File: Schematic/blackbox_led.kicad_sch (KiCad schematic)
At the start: 26 parts, among them U6 CSNP1GCR01-BOW

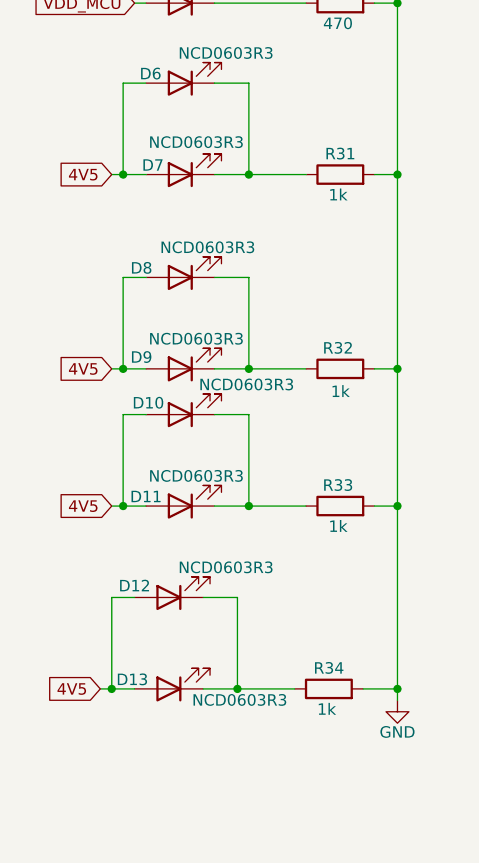
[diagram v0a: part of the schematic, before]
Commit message: optimisation : - refactoring two 4 pin connector for mag and gps into one 6 pin connector - increased output voltage from 5V buck regulator to take into account voltage decrease schottky diodes
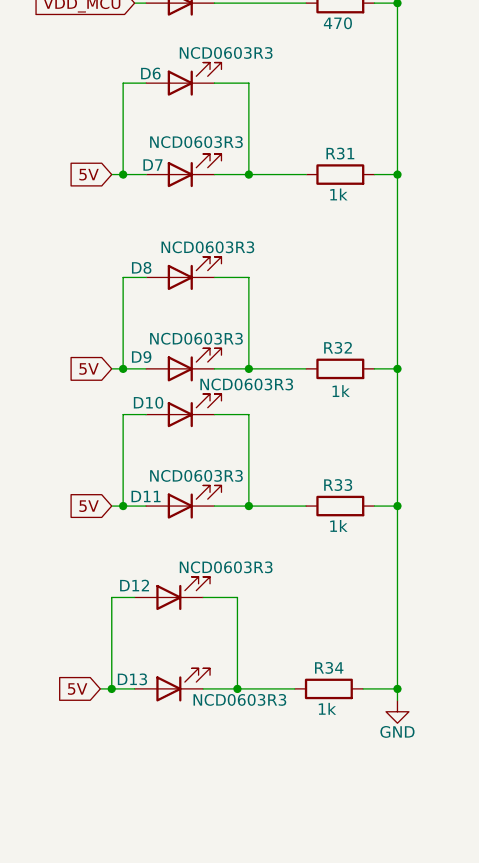
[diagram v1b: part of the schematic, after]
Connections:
- net 4V5 renamed 5V
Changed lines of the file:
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@@
 		)
 	)
-	(global_label "4V5"
+	(global_label "5V"
 		(shape input)
 		(at 58.42 97.79 180)
@@
 		)
 		(property "Intersheetrefs" "${INTERSHEET_REFS}"
-			(at 51.9272 97.79 0)
+			(at 53.1367 97.79 0)
 			(effects
 				(font
@@
 		)
 	)
-	(global_label "4V5"
+	(global_label "5V"
 		(shape input)
 		(at 58.42 119.38 180)
@@
 		)
 		(property "Intersheetrefs" "${INTERSHEET_REFS}"
-			(at 51.9272 119.38 0)
+			(at 53.1367 119.38 0)
 			(effects
 				(font
@@
 		)
 	)
-	(global_label "4V5"
+	(global_label "5V"
 		(shape input)
 		(at 57.15 154.94 180)
@@
 		)
 		(property "Intersheetrefs" "${INTERSHEET_REFS}"
-			(at 50.6572 154.94 0)
+			(at 51.8667 154.94 0)
 			(effects
 				(font
@@
 		)
 	)
-	(global_label "4V5"
+	(global_label "5V"
 		(shape input)
 		(at 58.42 134.62 180)
@@
 		)
 		(property "Intersheetrefs" "${INTERSHEET_REFS}"
-			(at 51.9272 134.62 0)
-			(effects
-				(font
+			(at 53.1367 134.62 0)
+			(effects
+				(font

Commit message: update on routing
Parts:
- C45, C46: footprint Capacitor_SMD:C_0603_1608Metric -> Capacitor_SMD:C_0402_1005Metric
- R28, R29, R30, R31, R32, R33, R34, R35, R36, R37, R38, R39: footprint Resistor_SMD:R_0603_1608Metric -> Resistor_SMD:R_0402_1005Metric
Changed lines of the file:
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@@
 			)
 		)
-		(property "Footprint" "Resistor_SMD:R_0603_1608Metric"
+		(property "Footprint" "Resistor_SMD:R_0402_1005Metric"
 			(at 232.918 109.22 90)
 			(effects
@@
 			)
 		)
-		(property "Footprint" "Resistor_SMD:R_0603_1608Metric"
+		(property "Footprint" "Resistor_SMD:R_0402_1005Metric"
 			(at 227.838 109.22 90)
 			(effects
@@
 			)
 		)
-		(property "Footprint" "Resistor_SMD:R_0603_1608Metric"
+		(property "Footprint" "Resistor_SMD:R_0402_1005Metric"
 			(at 83.82 136.398 90)
 			(effects
@@
 			)
 		)
-		(property "Footprint" "Resistor_SMD:R_0603_1608Metric"
+		(property "Footprint" "Resistor_SMD:R_0402_1005Metric"
 			(at 185.928 85.09 90)
 			(effects
@@
 			)
 		)
-		(property "Footprint" "Resistor_SMD:R_0603_1608Metric"
+		(property "Footprint" "Resistor_SMD:R_0402_1005Metric"
 			(at 82.55 156.718 90)
 			(effects
@@
 			)
 		)
-		(property "Footprint" "Resistor_SMD:R_0603_1608Metric"
+		(property "Footprint" "Resistor_SMD:R_0402_1005Metric"
 			(at 83.82 80.518 90)
 			(effects
@@
 			)
 		)
-		(property "Footprint" "Resistor_SMD:R_0603_1608Metric"
+		(property "Footprint" "Resistor_SMD:R_0402_1005Metric"
 			(at 83.82 58.928 90)
 			(effects
@@
 			)
 		)
-		(property "Footprint" "Resistor_SMD:R_0603_1608Metric"
+		(property "Footprint" "Resistor_SMD:R_0402_1005Metric"
 			(at 191.008 85.09 90)
 			(effects
@@
 			)
 		)
-		(property "Footprint" "Resistor_SMD:R_0603_1608Metric"
+		(property "Footprint" "Resistor_SMD:R_0402_1005Metric"
 			(at 237.998 109.22 90)
 			(effects
@@
 			)
 		)
-		(property "Footprint" "Capacitor_SMD:C_0603_1608Metric"
+		(property "Footprint" "Capacitor_SMD:C_0402_1005Metric"
 			(at 230.8352 88.9 0)
 			(effects
@@
 			)
 		)
-		(property "Footprint" "Resistor_SMD:R_0603_1608Metric"
+		(property "Footprint" "Resistor_SMD:R_0402_1005Metric"
 			(at 83.82 69.088 90)
 			(effects
@@
 			)
 		)
-		(property "Footprint" "Resistor_SMD:R_0603_1608Metric"
+		(property "Footprint" "Resistor_SMD:R_0402_1005Metric"
 			(at 83.82 121.158 90)
 			(effects
@@
 			)
 		)
-		(property "Footprint" "Capacitor_SMD:C_0603_1608Metric"
+		(property "Footprint" "Capacitor_SMD:C_0402_1005Metric"
 			(at 223.2152 88.9 0)
 			(effects
@@
 			)
 		)
-		(property "Footprint" "Resistor_SMD:R_0603_1608Metric"
+		(property "Footprint" "Resistor_SMD:R_0402_1005Metric"
 			(at 83.82 99.568 90)
 			(effects
